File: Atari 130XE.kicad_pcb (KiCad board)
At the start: 2 copper layers, 324.7 x 189 mm, 308 parts, among them J1 Power, J15 SIO_Port, J2 DIN-5_180degree, J3 Cartridge, J4 Joystick_Port, J5 Joystick_Port, J50 GTIA Fix, J51 OS Type, J52 Basic, J6 Keyboard, J7 SIMM_ON_OFF, Q1 2N3904, Q10 BC549, Q2 2N3904, Q3 2N3904, Q4 2N3906, Q6 2N3904, Q8 PN2222A, Q9 PN2222A, SW1 Switch_power_on, U1 PIA, U11 74LS74, U110 74AHC1G08, U111 74AHC1G08, U112 74AHC1G08, U113 74AHC1G08, U12 4050, U120 SIMM_exp_GAL, U121 DRAM_1MB_4bit, U122 DRAM_1MB_4bit, U123 74LS175, U124 74LS157, U13 74LS138, U14 MMU, U17 DRAM_4464, U18 DRAM_4464, U2 Antic, U21 NE555, U3 GTIA, U5 POKEY, U57 74HC14, U58 74LS175, U59 74HC74, U6 Sally, U60 74HC02, U61 74HC02, U62 4051, U63 4051, U7 27C512, U8 27C010, U9 Freddie, Y1 14,18757MHz, Y2 4.43MHz

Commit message: Global rebuild up to 1mB
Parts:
- removed C13, C14, C8, C9: 100nF, Capacitor_THT:C_Disc_D5.0mm_W2.5mm_P5.00mm
- removed C250: 22pF, Capacitor_SMD:C_1206_3216Metric_Pad1.42x1.75mm_HandSolder
- removed C254, C255: 100nF, Capacitor_SMD:C_1206_3216Metric_Pad1.42x1.75mm_HandSolder
- removed D50: BAS316, Atari:D_SOD-323_HandSoldering
- removed J50: GTIA Fix, Connector_PinHeader_2.54mm:PinHeader_2x08_P2.54mm_Vertical
- removed R206: 1k, Resistor_SMD:R_1206_3216Metric_Pad1.42x1.75mm_HandSolder
- removed U57: 74HC14, Package_SO:SOIC-14_3.9x8.7mm_P1.27mm
- removed U58: 74LS175, Package_SO:SOIC-16_3.9x9.9mm_P1.27mm
- moved C113 227.5 mm to (264.6, 108.4)
- moved U111 227.5 mm to (266.8, 104.8)
- moved R12 183.6 mm to (292.2, 107.0)
- moved U112 179.4 mm to (187.4, 82.5), turned to 90 degrees
- moved C106 179.1 mm to (187.2, 79.2)
- moved U13 155.1 mm to (271.7, 111.1), turned to 90 degrees
- moved R154 138.2 mm to (107.0, 105.0)
- moved R155 138.2 mm to (112.9, 105.0)
- moved J7 138.2 mm to (99.1, 105.7)
- moved C26 110.9 mm to (271.8, 100.0)
- moved C24 69.7 mm to (66.4, 175.8)
- moved C25 69.7 mm to (63.3, 168.6)
- moved U120 55.3 mm to (110.6, 122.8), turned to 0 degrees
- moved U123 51.0 mm to (121.5, 159.9), turned to 180 degrees
- moved C18 47.2 mm to (111.6, 166.6), turned to 0 degrees
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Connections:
- C206 pad 1: GTIA_NORM -> Net-(C206-Pad1)
- FB3 pad 1: GTIA_NORM -> Net-(C206-Pad1)
- U11 pad 3: GTIA_NORM -> Net-(C206-Pad1)
- U3 pad 18: GTIA_AN0 -> AN0
- U3 pad 19: GTIA_AN1 -> AN1
- U3 pad 20: GTIA_AN2 -> AN2
- U3 pad 28: GTIA_OSC -> Net-(C206-Pad1)
- U61 pad 8: O2 -> BO2
- U61 pad 9: O2 -> BO2
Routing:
- net GTIA_OSC: track 108.3 -> 0.00 mm, vias 2 -> 0
- net AN2: track 96.2 -> 0.00 mm, vias 2 -> 0
- net AN1: track 87.5 -> 0.00 mm, vias 1 -> 0
- net AN0: track 85.7 -> 0.00 mm
- net GTIA_AN0: track 75.4 -> 0.00 mm
- net GTIA_AN1: track 72.1 -> 0.00 mm
- net GTIA_AN2: track 69.7 -> 0.00 mm
- net VCC: track 952.9 -> 896.2 mm, vias 21 -> 17
- net GND: track 507.1 -> 476.4 mm, vias 224 -> 126
- net Net-(C250-Pad2): track 15.1 -> 0.00 mm
- net AN2_FIX: track 14.7 -> 0.00 mm, vias 2 -> 0
- net AN0_FIX: track 14.6 -> 0.00 mm
- net POKEY: track 36.5 -> 22.3 mm, vias 2 -> 1
- net Net-(D50-Pad2): track 13.4 -> 0.00 mm
- net OSC: track 10.6 -> 0.00 mm
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
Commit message: memory track
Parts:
- removed U3: GTIA, Package_DIP:DIP-40_W15.24mm_LongPads
- moved R1 20.7 mm to (56.4, 193.4)
- moved C23 4.99 mm to (59.1, 192.0), turned to 270 degrees
- moved C10 3.72 mm to (83.9, 153.8)
- moved C17 3.54 mm to (83.9, 137.7)
- moved C16 2.56 mm to (89.0, 119.6)
- moved C15 1.62 mm to (89.0, 107.6)
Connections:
- U121 pad 15: (no net) -> Net-(U121-Pad15)
- U121 pad 5: (no net) -> Net-(U121-Pad5)
- U122 pad 15: Net-(U122-Pad15) -> Net-(U121-Pad15)
- U122 pad 5: Net-(U122-Pad5) -> Net-(U121-Pad5)
- U124 pad 4: Net-(U122-Pad15) -> Net-(U121-Pad15)
- U124 pad 7: Net-(U122-Pad5) -> Net-(U121-Pad5)
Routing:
- net A0: track 393.2 -> 555.1 mm
- net A1: track 367.6 -> 524.1 mm
- net A2: track 351.3 -> 502.4 mm
- net RA7: track 0.00 -> 147.5 mm, vias 0 -> 2
- net A3: track 329.0 -> 474.2 mm
- net A4: track 208.7 -> 348.0 mm
- net A10: track 254.0 -> 391.6 mm, vias 4 -> 6
- net A8: track 160.8 -> 296.0 mm, vias 2 -> 4
- net A9: track 172.5 -> 307.4 mm, vias 4 -> 6
- net A5: track 197.9 -> 331.3 mm
- net A11: track 190.3 -> 323.6 mm, vias 3 -> 5
- net A13: track 186.9 -> 317.4 mm
- net RA6: track 0.00 -> 130.0 mm
- net A6: track 82.1 -> 209.7 mm
- net RA5: track 0.00 -> 127.1 mm
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
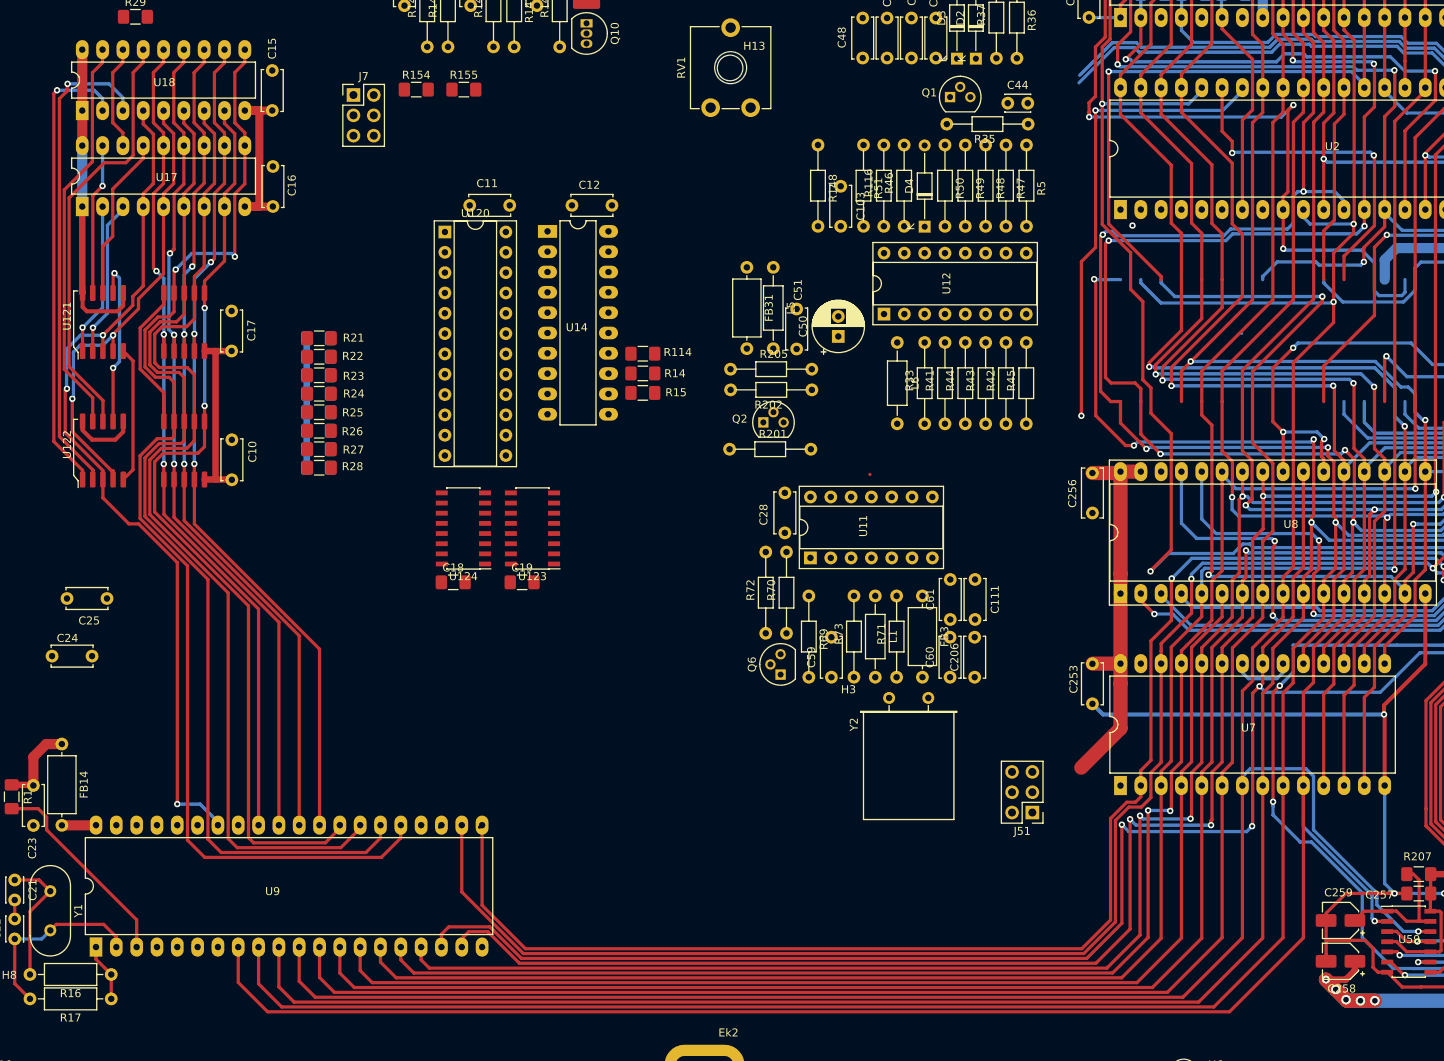
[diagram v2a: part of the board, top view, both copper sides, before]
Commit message: memory connection
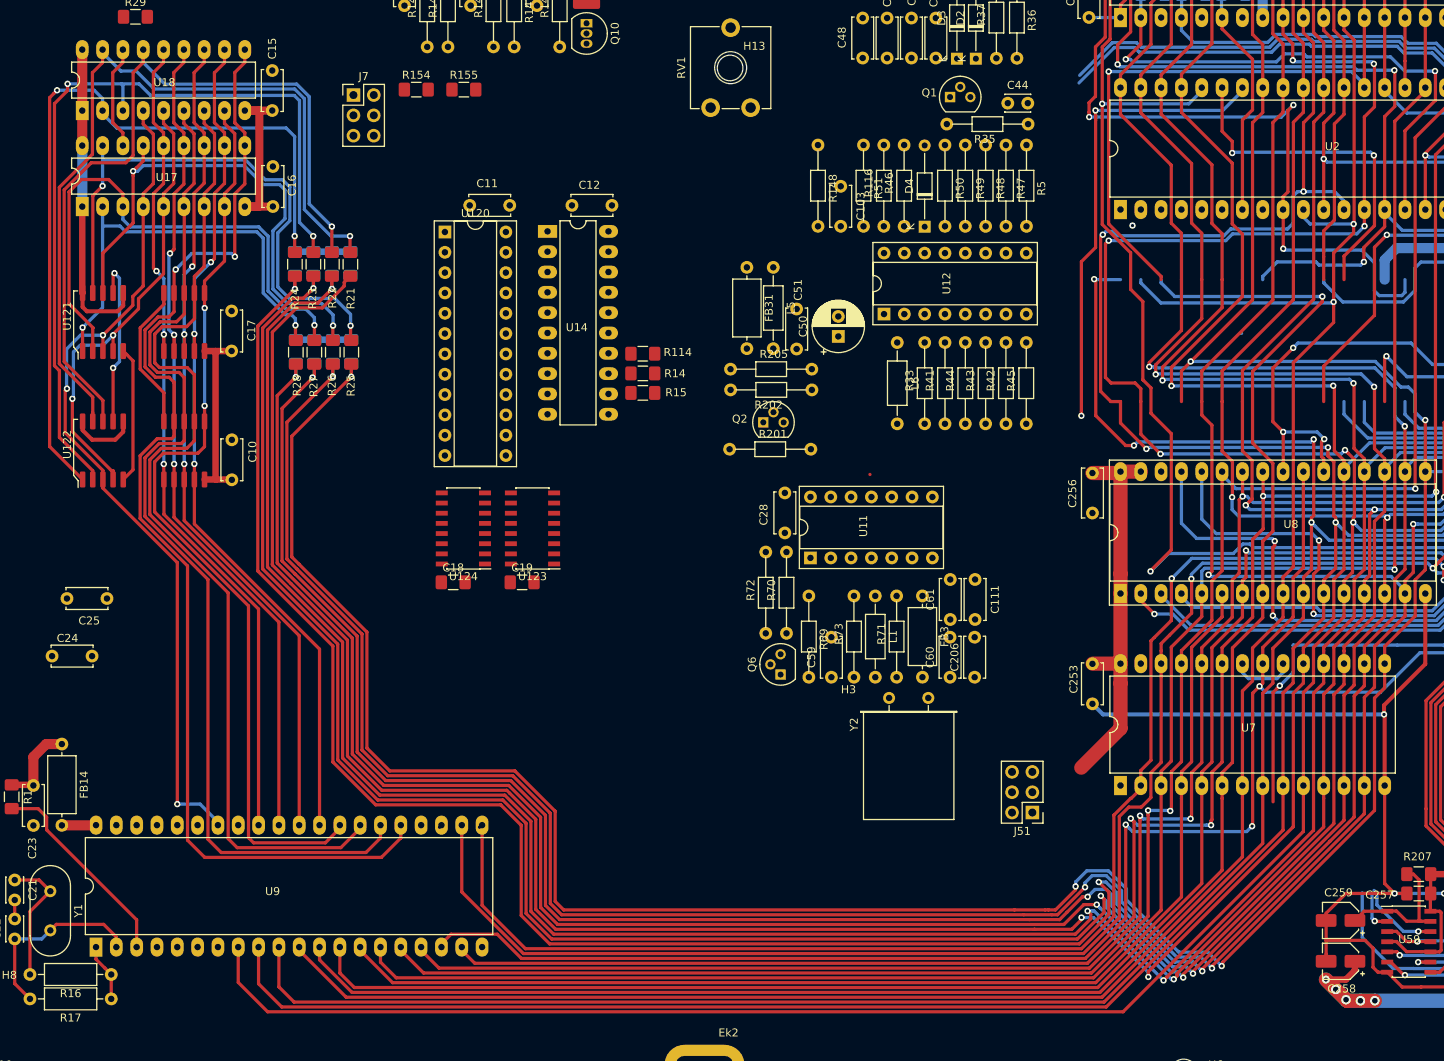
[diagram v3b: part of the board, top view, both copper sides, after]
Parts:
- moved R103 16.5 mm to (91.8, 126.8), turned to 270 degrees
- moved R24 16.5 mm to (91.8, 126.8), turned to 270 degrees
- moved R107 14.8 mm to (91.9, 137.8), turned to 270 degrees
- moved R28 14.7 mm to (91.9, 137.8), turned to 270 degrees
- moved R102 14.0 mm to (94.1, 126.8), turned to 270 degrees
- moved R23 13.9 mm to (94.1, 126.8), turned to 270 degrees
- moved R106 12.2 mm to (94.2, 137.8), turned to 270 degrees
- moved R27 12.1 mm to (94.2, 137.8), turned to 270 degrees
- moved R101 11.8 mm to (96.4, 126.8), turned to 270 degrees
- moved R22 11.7 mm to (96.4, 126.8), turned to 270 degrees
- moved R100 10.1 mm to (98.7, 126.8), turned to 270 degrees
- moved R105 10.1 mm to (96.5, 137.8), turned to 270 degrees
- moved R21 10.0 mm to (98.7, 126.8), turned to 270 degrees
- moved R26 9.96 mm to (96.5, 137.8), turned to 270 degrees
- moved R104 8.61 mm to (98.9, 137.8), turned to 270 degrees
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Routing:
- net D4: track 273.5 -> 526.1 mm, vias 3 -> 6
- net D5: track 276.2 -> 523.4 mm, vias 4 -> 7
- net D6: track 280.4 -> 523.4 mm, vias 4 -> 7
- net D7: track 277.9 -> 514.8 mm, vias 4 -> 6
- net D3: track 247.6 -> 480.6 mm, vias 4 -> 7
- net D2: track 283.3 -> 499.5 mm, vias 3 -> 6
- net D1: track 291.7 -> 505.4 mm, vias 6 -> 9
- net D0: track 327.5 -> 537.8 mm, vias 5 -> 8
- net DQ3: track 19.4 -> 71.4 mm, vias 1 -> 2
- net DQ7: track 49.9 -> 101.4 mm, vias 0 -> 1
- net DQ1: track 19.6 -> 68.7 mm
- net DQ6: track 53.6 -> 99.9 mm, vias 0 -> 1
- net DQ2: track 20.5 -> 66.1 mm, vias 0 -> 2
- net DQ5: track 61.3 -> 105.9 mm, vias 1 -> 2
- net DQ4: track 58.4 -> 98.9 mm, vias 1 -> 2
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
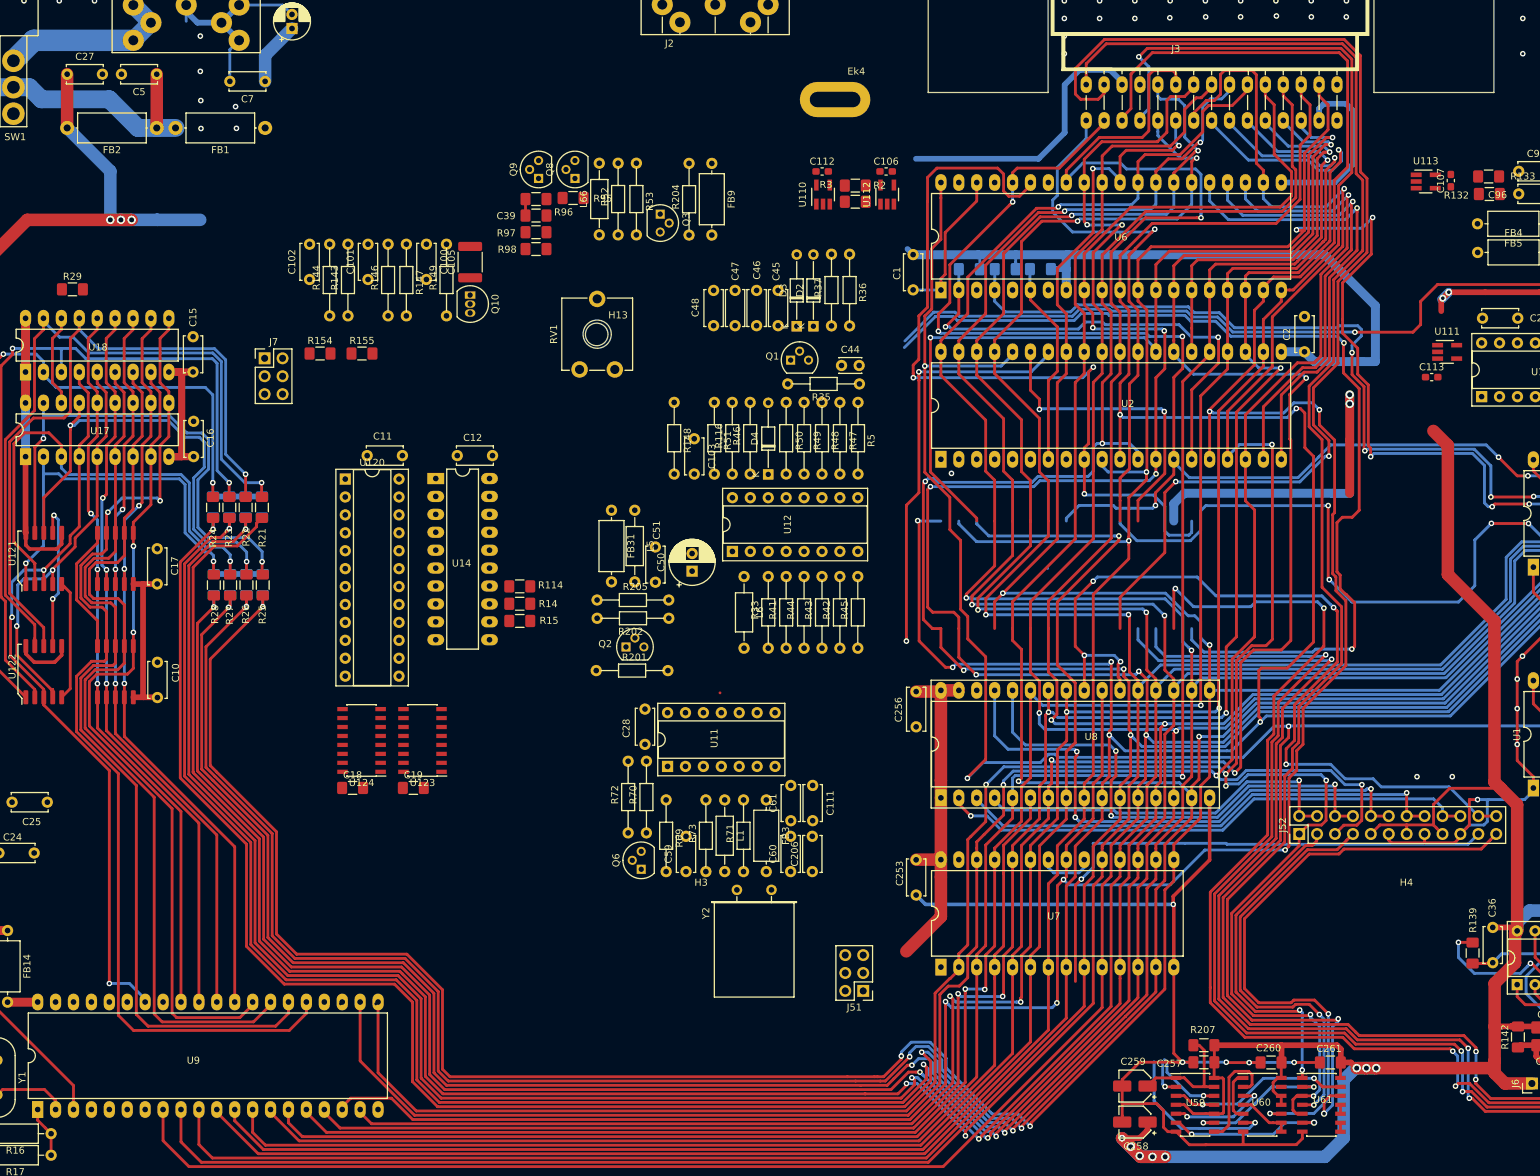
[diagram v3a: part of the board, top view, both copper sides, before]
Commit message: SIMM exp route
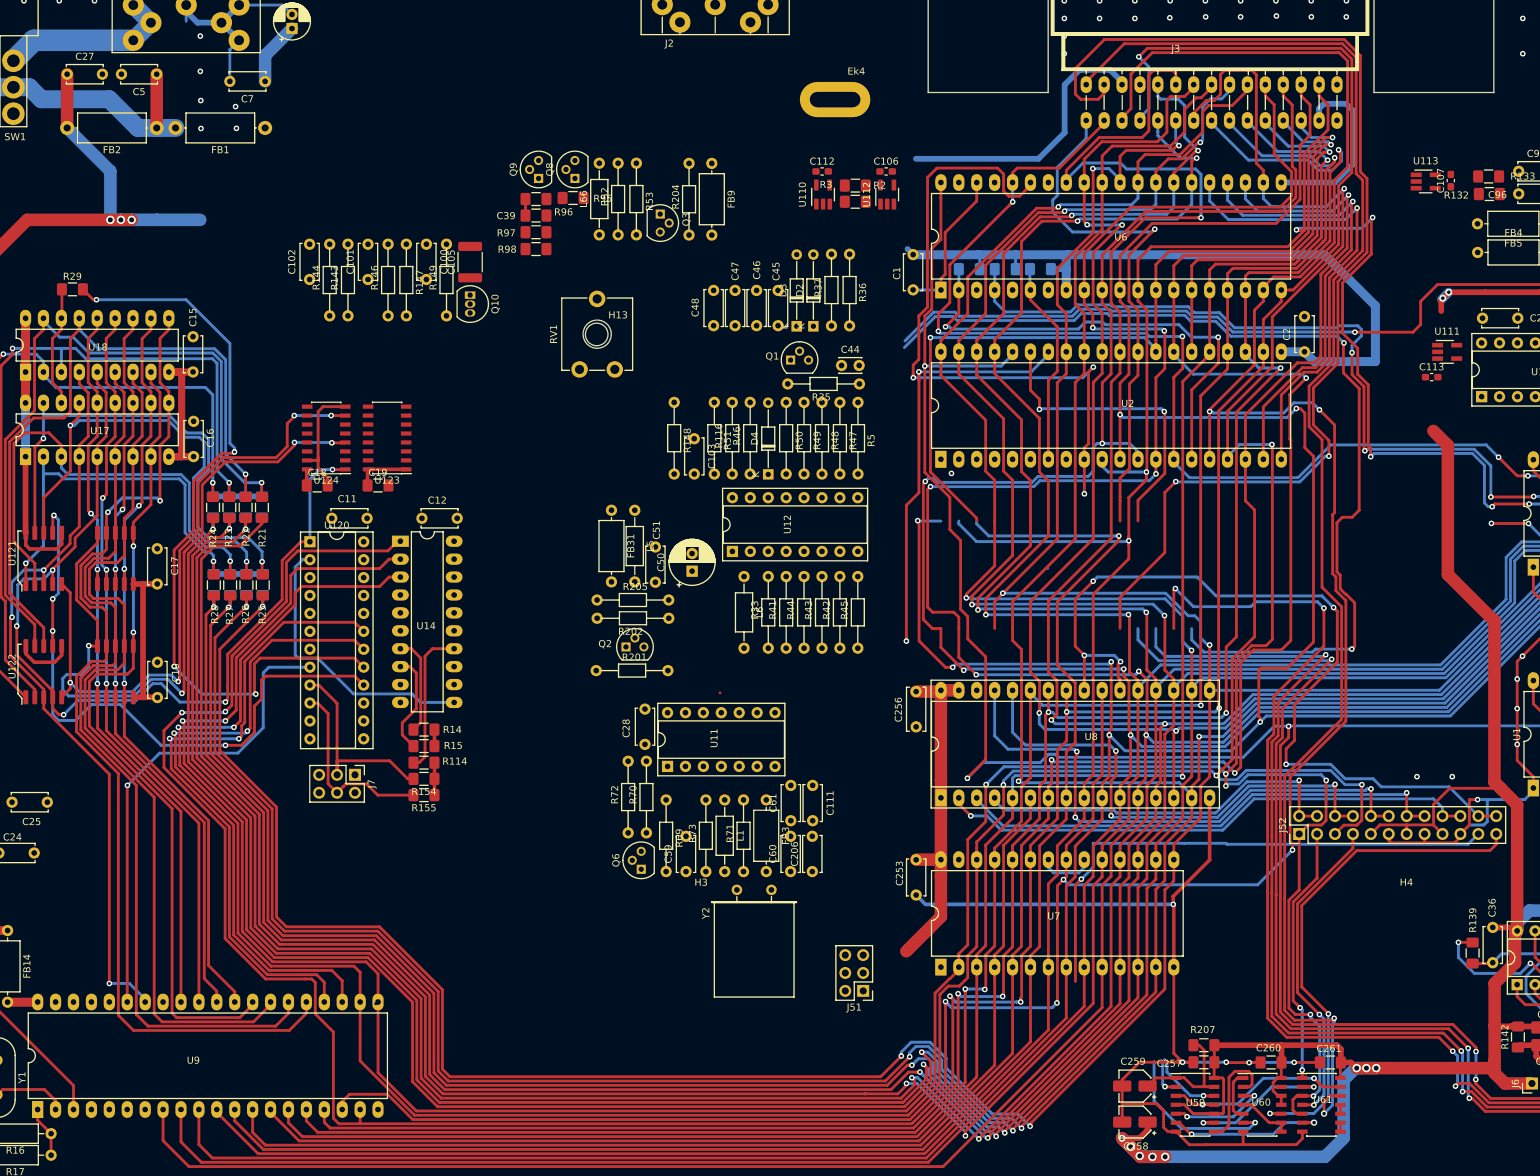
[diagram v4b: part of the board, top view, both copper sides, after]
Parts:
- moved R155 63.2 mm to (121.7, 167.6), turned to 180 degrees
- moved R154 62.1 mm to (121.7, 165.3), turned to 180 degrees
- moved J7 60.4 mm to (111.9, 164.7), turned to 270 degrees
- moved U123 43.2 mm to (116.5, 117.0)
- moved U124 43.2 mm to (107.9, 117.0)
- moved C18 43.2 mm to (106.6, 123.7)
- moved C19 43.2 mm to (115.2, 123.7)
- moved R114 28.4 mm to (121.7, 163.0)
- moved R14 22.4 mm to (121.7, 158.3)
- moved R15 22.3 mm to (121.7, 160.7)
- moved C11 10.2 mm to (113.6, 128.4)
- moved C12 10.2 mm to (126.4, 128.4)
- moved U120 10.2 mm to (105.5, 131.7)
- moved U14 10.2 mm to (118.4, 131.6)
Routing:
- net A11: track 321.4 -> 447.2 mm, vias 5 -> 7
- net CASMAN: track 0.00 -> 108.5 mm, vias 0 -> 4
- net A13: track 317.4 -> 420.3 mm, vias 4 -> 6
- net A12: track 407.5 -> 503.2 mm, vias 9 -> 11
- net FA14: track 0.00 -> 91.6 mm, vias 1 -> 2
- net FA15: track 0.00 -> 91.4 mm, vias 0 -> 2
- net Net-(U121-Pad15): track 18.5 -> 101.7 mm, vias 0 -> 4
- net BO2: track 211.5 -> 133.6 mm, vias 5 -> 3
- net Net-(U121-Pad5): track 17.1 -> 90.4 mm, vias 0 -> 4
- net RAS: track 57.8 -> 130.0 mm, vias 2 -> 5
- net CAS: track 0.00 -> 68.1 mm, vias 0 -> 1
- net CAS_SIMM: track 21.7 -> 89.6 mm, vias 2 -> 4
- net +5VA: track 52.4 -> 9.07 mm, vias 2 -> 0
- net REF: track 0.00 -> 40.3 mm
- net SIMM_I8: track 0.00 -> 28.9 mm
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
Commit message: Track
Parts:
- added U3: GTIA, Package_DIP:DIP-40_W15.24mm_LongPads, F.Cu at (195.0, 144.2)
- U120: footprint Package_DIP:DIP-24_W7.62mm_Socket -> Package_DIP:DIP-24_W7.62mm_Socket_LongPads
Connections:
- U120 pad 11: (no net) -> Net-(U120-Pad11)
- U120 pad 20: (no net) -> Net-(U120-Pad20)
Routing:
- net PB7: track 3.40 -> 353.2 mm, vias 0 -> 4
- net PB6: track 3.40 -> 348.3 mm, vias 0 -> 3
- net PB1: track 3.41 -> 337.0 mm, vias 0 -> 4
- net PB5: track 3.41 -> 332.6 mm, vias 0 -> 3
- net PB2: track 3.40 -> 290.6 mm, vias 0 -> 2
- net PB3: track 3.40 -> 289.9 mm, vias 0 -> 2
- net PB4: track 3.40 -> 287.7 mm, vias 0 -> 2
- net PB0: track 3.42 -> 282.2 mm, vias 0 -> 2
- net O2: track 0.00 -> 137.1 mm, vias 0 -> 2
- net CASINH: track 0.00 -> 119.7 mm, vias 0 -> 1
- net RAS: track 130.0 -> 179.2 mm, vias 5 -> 6
- net Net-(U120-Pad15): track 0.00 -> 48.8 mm, vias 0 -> 1
- net VCC: track 964.6 -> 1003.6 mm
- net BE: track 0.00 -> 29.7 mm, vias 0 -> 1
- net GND: track 546.0 -> 575.7 mm, vias 126 -> 122
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
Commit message: Tracking
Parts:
- J52: value Basic -> Conn_02x08_Odd_Even; footprint Connector_PinHeader_2.54mm:PinHeader_2x12_P2.54mm_Vertical -> Connector_PinHeader_2.54mm:PinHeader_2x08_P2.54mm_Vertical
- moved J52 3.06 mm to (248.9, 173.2)
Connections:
- J52 pad 10: A14_sel -> A15_sel
- J52 pad 12: A14_sel -> A15_sel
- J52 pad 14: A15_sel -> A14_sel
- J52 pad 16: A15_sel -> A14_sel
- J52 pad 5: A13 -> VCC
- J52 pad 6: A13_sel -> A16_sel
- J52 pad 7: A13_cart -> GND
- J52 pad 8: A13_sel -> A16_sel
- U120 pad 11: Net-(U120-Pad11) -> (no net)
- U120 pad 20: Net-(U120-Pad20) -> (no net)
- U8 pad 22: BASIC_sel -> BASC_cart
- U8 pad 24: BASIC_sel -> BASC_cart
- U8 pad 28: A13_sel -> A13_cart
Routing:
- net BASIC: track 98.8 -> 221.3 mm, vias 2 -> 4
- net BASIC_sel: track 121.3 -> 0.00 mm, vias 5 -> 0
- net Net-(R44-Pad2): track 0.00 -> 87.6 mm
- net Net-(L6-Pad1): track 0.00 -> 85.9 mm
- net Net-(R42-Pad2): track 0.00 -> 78.0 mm
- net Net-(R43-Pad2): track 0.00 -> 73.1 mm
- net A13_sel: track 72.0 -> 0.00 mm, vias 3 -> 0
- net AN1: track 0.00 -> 67.9 mm, vias 0 -> 2
- net Net-(U12-Pad14): track 0.00 -> 67.8 mm
- net AN0: track 0.00 -> 66.5 mm, vias 0 -> 2
- net AN2: track 0.00 -> 64.5 mm, vias 0 -> 2
- net BASC_cart: track 72.4 -> 14.8 mm
- net A13_cart: track 45.5 -> 0.00 mm, vias 2 -> 0
- net A10: track 391.6 -> 346.2 mm, vias 6 -> 4
- net GND: track 575.7 -> 534.3 mm, vias 122 -> 119
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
